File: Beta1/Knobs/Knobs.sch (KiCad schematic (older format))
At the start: 32 parts, among them U1000 MCP3008T-I/SL, U2 MCP3008T-I/SL

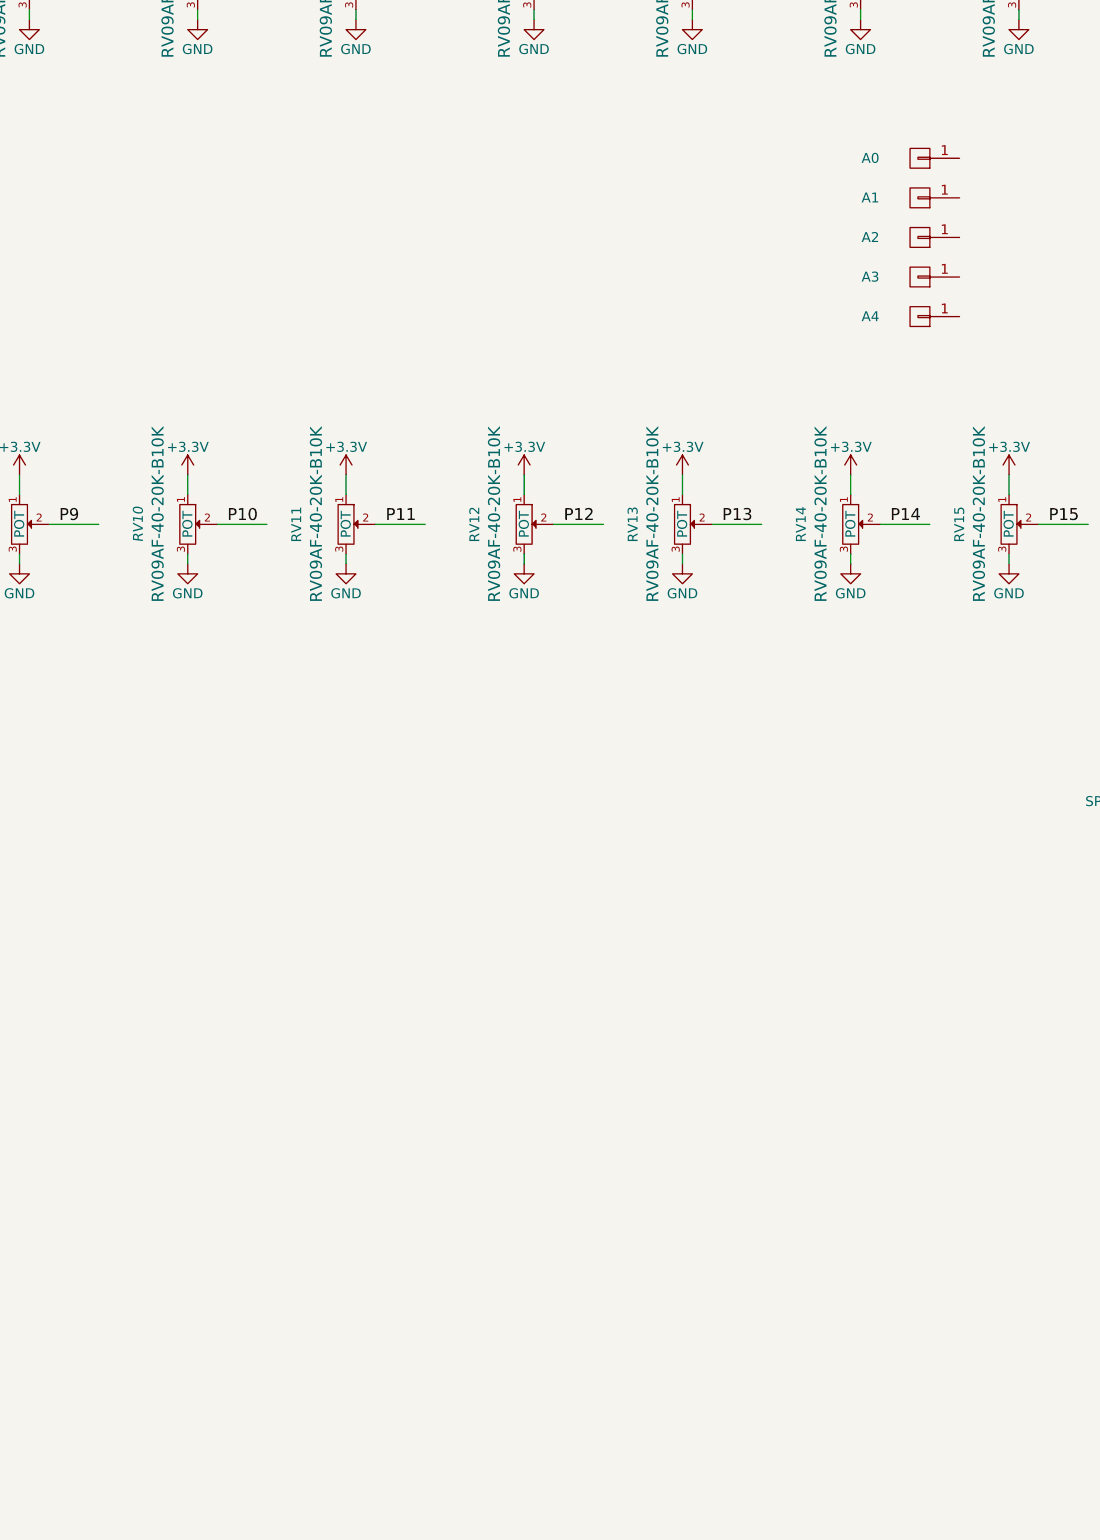
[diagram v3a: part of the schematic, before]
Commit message: Added volume knob + XY Joy to Knobs 16 CH Board.
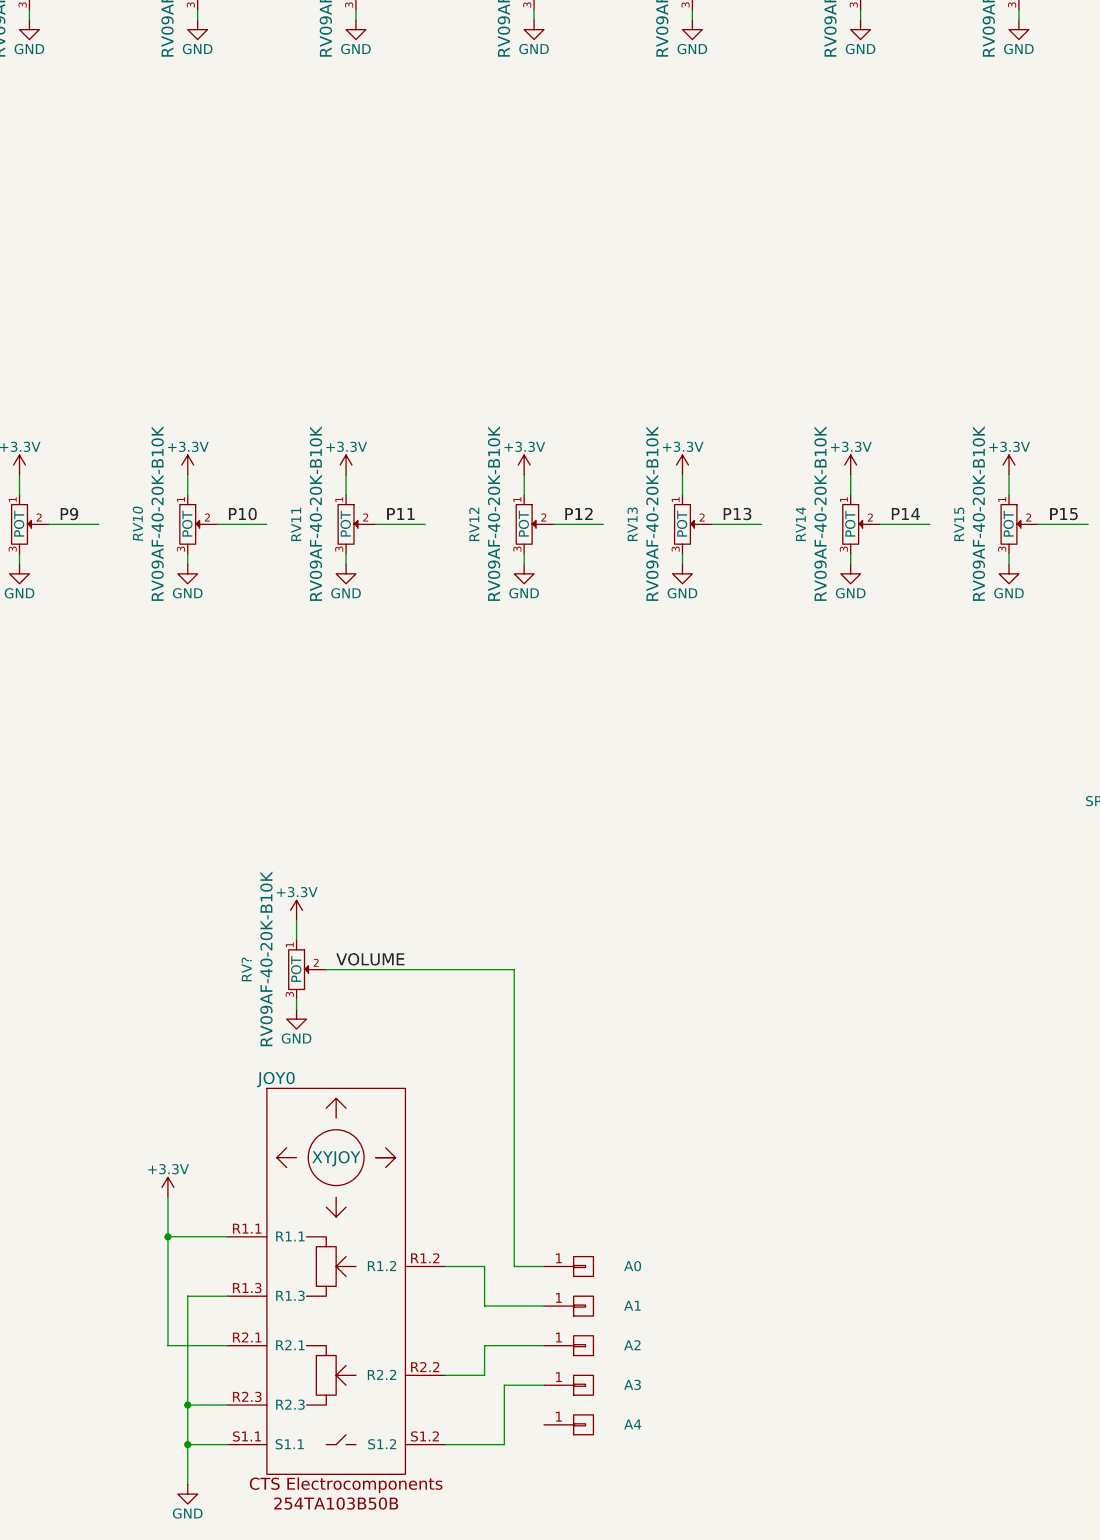
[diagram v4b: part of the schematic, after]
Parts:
- added JOY0: XYJOY, Liberry:XY_JOY_254TA103B50B, symbol XYJOY
- added RV?: POT, Liberry:RV09AF-40-20K-B10K, symbol POT
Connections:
- net labels added: VOLUME
- wire segments 92 -> 113
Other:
- moved on the sheet: A0, A1, A2, A3, A4
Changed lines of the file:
@@
 Text Label 11350 1750 0    60   ~ 0
 MISO
+Text Label 11450 4500 0    60   ~ 0
+MISO
+$Comp
+L CONN_01X01 A0
+U 1 1 58336F43
+P 5750 8050
+F 0 "A0" H 6000 8050 50  0000 C CNN
+F 1 "CONN_01X01" V 5850 8050 50  0001 C CNN
+F 2 "Liberry:TH_0.1_1x2_Jumper" H 5750 8050 50  0001 C CNN
+F 3 "" H 5750 8050 50  0000 C CNN
+F 4 "PCB" H 5750 8050 60  0001 C CNN "MFG"
+F 5 "ON_PCB" H 5750 8050 60  0001 C CNN "MPN"
+	1    5750 8050
+	1    0    0    1
+$EndComp
+$Comp
+L CONN_01X01 A1
+U 1 1 5833717C
+P 5750 8250
+F 0 "A1" H 6000 8250 50  0000 C CNN
+F 1 "CONN_01X01" V 5850 8250 50  0001 C CNN
+F 2 "Liberry:TH_0.1_1x2_Jumper" H 5750 8250 50  0001 C CNN
+F 3 "" H 5750 8250 50  0000 C CNN
+F 4 "PCB" H 5750 8250 60  0001 C CNN "MFG"
+F 5 "ON_PCB" H 5750 8250 60  0001 C CNN "MPN"
+	1    5750 8250
+	1    0    0    1
+$EndComp
+$Comp
+L CONN_01X01 A2
+U 1 1 58337609
+P 5750 8450
+F 0 "A2" H 6000 8450 50  0000 C CNN
+F 1 "CONN_01X01" V 5850 8450 50  0001 C CNN
+F 2 "Liberry:TH_0.1_1x2_Jumper" H 5750 8450 50  0001 C CNN
+F 3 "" H 5750 8450 50  0000 C CNN
+F 4 "PCB" H 5750 8450 60  0001 C CNN "MFG"
+F 5 "ON_PCB" H 5750 8450 60  0001 C CNN "MPN"
+	1    5750 8450
+	1    0    0    1
+$EndComp
+$Comp
+L CONN_01X01 A3
+U 1 1 58337619
+P 5750 8650
+F 0 "A3" H 6000 8650 50  0000 C CNN
+F 1 "CONN_01X01" V 5850 8650 50  0001 C CNN
+F 2 "Liberry:TH_0.1_1x2_Jumper" H 5750 8650 50  0001 C CNN
+F 3 "" H 5750 8650 50  0000 C CNN
+F 4 "PCB" H 5750 8650 60  0001 C CNN "MFG"
+F 5 "ON_PCB" H 5750 8650 60  0001 C CNN "MPN"
+	1    5750 8650
+	1    0    0    1
+$EndComp
+$Comp
+L CONN_01X01 A4
+U 1 1 58337C21
+P 5750 8850
+F 0 "A4" H 6000 8850 50  0000 C CNN
+F 1 "CONN_01X01" V 5850 8850 50  0001 C CNN
+F 2 "Liberry:TH_0.1_1x2_Jumper" H 5750 8850 50  0001 C CNN
+F 3 "" H 5750 8850 50  0000 C CNN
+F 4 "PCB" H 5750 8850 60  0001 C CNN "MFG"
+F 5 "ON_PCB" H 5750 8850 60  0001 C CNN "MPN"
+	1    5750 8850
+	1    0    0    1
+$EndComp
+$Comp
+L XYJOY JOY0
+U 1 1 5880F7E5
+P 4500 8050
+F 0 "JOY0" H 4200 9000 60  0000 C CNN
+F 1 "XYJOY" H 4500 8600 60  0000 C CNN
+F 2 "Liberry:XY_JOY_254TA103B50B" H 4500 8600 60  0001 C CNN
+F 3 "" H 4500 8600 60  0001 C CNN
+	1    4500 8050
+	1    0    0    -1
+$EndComp
+$Comp
+L +3.3V #PWR?
+U 1 1 5880F86D
+P 3650 7700
+F 0 "#PWR?" H 3650 7550 50  0001 C CNN
+F 1 "+3.3V" H 3650 7840 50  0000 C CNN
+F 2 "" H 3650 7700 50  0000 C CNN
+F 3 "" H 3650 7700 50  0000 C CNN
+	1    3650 7700
+	1    0    0    -1
+$EndComp
+$Comp
+L GND #PWR?
+U 1 1 5880F8DB
+P 3750 9150
+F 0 "#PWR?" H 3750 8900 50  0001 C CNN
+F 1 "GND" H 3750 9000 50  0000 C CNN
+F 2 "" H 3750 9150 50  0000 C CNN
+F 3 "" H 3750 9150 50  0000 C CNN
+	1    3750 9150
+	1    0    0    -1
+$EndComp
 Wire Wire Line
 	2150 1400 2150 1300
@@
 Wire Wire Line
 	11150 4500 12000 4500
-Text Label 11450 4500 0    60   ~ 0
-MISO
-$Comp
-L CONN_01X01 A0
-U 1 1 58336F43
-P 7450 2450
-F 0 "A0" H 7700 2450 50  0000 C CNN
-F 1 "CONN_01X01" V 7550 2450 50  0001 C CNN
-F 2 "Liberry:TH_0.1_1x2_Jumper" H 7450 2450 50  0001 C CNN
-F 3 "" H 7450 2450 50  0000 C CNN
-F 4 "PCB" H 7450 2450 60  0001 C CNN "MFG"
-F 5 "ON_PCB" H 7450 2450 60  0001 C CNN "MPN"
-	1    7450 2450
-	-1   0    0    1
-$EndComp
-$Comp
-L CONN_01X01 A1
-U 1 1 5833717C
-P 7450 2650
-F 0 "A1" H 7700 2650 50  0000 C CNN
-F 1 "CONN_01X01" V 7550 2650 50  0001 C CNN
-F 2 "Liberry:TH_0.1_1x2_Jumper" H 7450 2650 50  0001 C CNN
-F 3 "" H 7450 2650 50  0000 C CNN
-F 4 "PCB" H 7450 2650 60  0001 C CNN "MFG"
-F 5 "ON_PCB" H 7450 2650 60  0001 C CNN "MPN"
-	1    7450 2650
-	-1   0    0    1
-$EndComp
-$Comp
-L CONN_01X01 A2
-U 1 1 58337609
-P 7450 2850
-F 0 "A2" H 7700 2850 50  0000 C CNN
-F 1 "CONN_01X01" V 7550 2850 50  0001 C CNN
-F 2 "Liberry:TH_0.1_1x2_Jumper" H 7450 2850 50  0001 C CNN
-F 3 "" H 7450 2850 50  0000 C CNN
-F 4 "PCB" H 7450 2850 60  0001 C CNN "MFG"
-F 5 "ON_PCB" H 7450 2850 60  0001 C CNN "MPN"
-	1    7450 2850
-	-1   0    0    1
-$EndComp
-$Comp
-L CONN_01X01 A3
-U 1 1 58337619
-P 7450 3050
-F 0 "A3" H 7700 3050 50  0000 C CNN
-F 1 "CONN_01X01" V 7550 3050 50  0001 C CNN
-F 2 "Liberry:TH_0.1_1x2_Jumper" H 7450 3050 50  0001 C CNN
-F 3 "" H 7450 3050 50  0000 C CNN
-F 4 "PCB" H 7450 3050 60  0001 C CNN "MFG"
-F 5 "ON_PCB" H 7450 3050 60  0001 C CNN "MPN"
-	1    7450 3050
-	-1   0    0    1
-$EndComp
-$Comp
-L CONN_01X01 A4
-U 1 1 58337C21
-P 7450 3250
-F 0 "A4" H 7700 3250 50  0000 C CNN
-F 1 "CONN_01X01" V 7550 3250 50  0001 C CNN
-F 2 "Liberry:TH_0.1_1x2_Jumper" H 7450 3250 50  0001 C CNN
-F 3 "" H 7450 3250 50  0000 C CNN
-F 4 "PCB" H 7450 3250 60  0001 C CNN "MFG"
-F 5 "ON_PCB" H 7450 3250 60  0001 C CNN "MPN"
-	1    7450 3250
-	-1   0    0    1
-$EndComp
+Wire Wire Line
+	3950 7900 3650 7900
+Wire Wire Line
+	3650 7700 3650 8450
+Wire Wire Line
+	3650 8450 3950 8450
+Connection ~ 3650 7900
+Wire Wire Line
+	3950 8200 3750 8200
+Wire Wire Line
+	3750 8200 3750 9150
+Wire Wire Line
+	3950 8750 3750 8750
+Connection ~ 3750 8750
+Wire Wire Line
+	3950 8950 3750 8950
+Connection ~ 3750 8950
+$Comp
+L POT RV?
+U 1 1 58810DA5
+P 4300 6550
+F 0 "RV?" H 4300 6300 50  0000 C CNN
+F 1 "POT" H 4300 6550 50  0000 C CNN
+F 2 "Liberry:RV09AF-40-20K-B10K" H 4300 6550 50  0001 C CNN
+F 3 "" H 4300 6550 50  0000 C CNN
+F 4 "Alpha Taiwan" H 4300 6550 60  0001 C CNN "MFG"
+F 5 "RV09AF-40-20K-B10K" H 4250 6400 60  0000 C CNN "MPN"
+	1    4300 6550
+	0    1    1    0
+$EndComp
+$Comp
+L GND #PWR?
+U 1 1 58810DAB
+P 4300 6750
+F 0 "#PWR?" H 4300 6500 50  0001 C CNN
+F 1 "GND" H 4300 6600 50  0000 C CNN
+F 2 "" H 4300 6750 50  0000 C CNN
+F 3 "" H 4300 6750 50  0000 C CNN
+	1    4300 6750
+	1    0    0    -1
+$EndComp
+$Comp
+L +3.3V #PWR?
+U 1 1 58810DB1
+P 4300 6300
+F 0 "#PWR?" H 4300 6150 50  0001 C CNN
+F 1 "+3.3V" H 4300 6440 50  0000 C CNN
+F 2 "" H 4300 6300 50  0000 C CNN
+F 3 "" H 4300 6300 50  0000 C CNN
+	1    4300 6300
+	1    0    0    -1
+$EndComp
+Text Label 4500 6550 0    60   ~ 0
+VOLUME
+Wire Wire Line
+	4300 6400 4300 6300
+Wire Wire Line
+	4300 6750 4300 6700
+Wire Wire Line
+	4450 6550 5400 6550
+Wire Wire Line
+	5400 6550 5400 8050
+Wire Wire Line
+	5400 8050 5550 8050
+Wire Wire Line
+	5050 8050 5250 8050
+Wire Wire Line
+	5250 8050 5250 8250
+Wire Wire Line
+	5250 8250 5550 8250
+Wire Wire Line
+	5050 8600 5250 8600
+Wire Wire Line
+	5250 8600 5250 8450
+Wire Wire Line
+	5250 8450 5550 8450
+Wire Wire Line
+	5050 8950 5350 8950
+Wire Wire Line
+	5350 8950 5350 8650
+Wire Wire Line
+	5350 8650 5550 8650
 $EndSCHEMATC

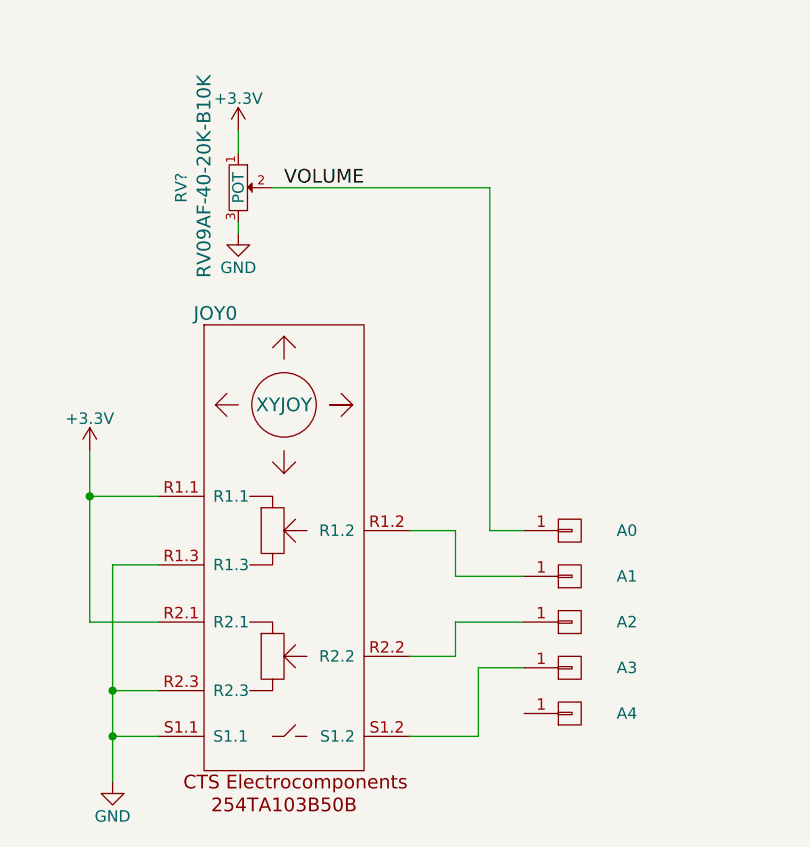
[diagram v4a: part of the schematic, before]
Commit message: Reduced width by 5.08. Changed pinout location and organization
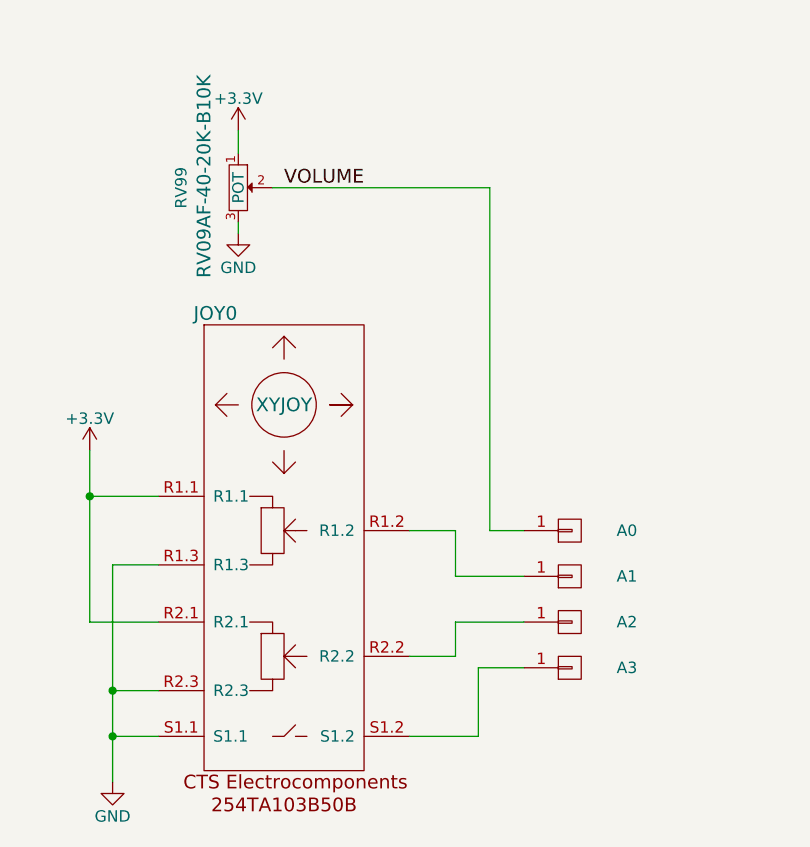
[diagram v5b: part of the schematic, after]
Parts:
- removed A4: CONN_01X01, Liberry:TH_0.1_1x2_Jumper, symbol CONN_01X01
- A0, A1, A2, A3: footprint Liberry:TH_0.1_1x2_Jumper -> Liberry:single_0.1
- gave numbers to parts that had none: 1
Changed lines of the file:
@@
 F 0 "A0" H 6000 8050 50  0000 C CNN
 F 1 "CONN_01X01" V 5850 8050 50  0001 C CNN
-F 2 "Liberry:TH_0.1_1x2_Jumper" H 5750 8050 50  0001 C CNN
+F 2 "Liberry:single_0.1" H 5750 8050 50  0001 C CNN
 F 3 "" H 5750 8050 50  0000 C CNN
 F 4 "PCB" H 5750 8050 60  0001 C CNN "MFG"
@@
 F 0 "A1" H 6000 8250 50  0000 C CNN
 F 1 "CONN_01X01" V 5850 8250 50  0001 C CNN
-F 2 "Liberry:TH_0.1_1x2_Jumper" H 5750 8250 50  0001 C CNN
+F 2 "Liberry:single_0.1" H 5750 8250 50  0001 C CNN
 F 3 "" H 5750 8250 50  0000 C CNN
 F 4 "PCB" H 5750 8250 60  0001 C CNN "MFG"
@@
 F 0 "A2" H 6000 8450 50  0000 C CNN
 F 1 "CONN_01X01" V 5850 8450 50  0001 C CNN
-F 2 "Liberry:TH_0.1_1x2_Jumper" H 5750 8450 50  0001 C CNN
+F 2 "Liberry:single_0.1" H 5750 8450 50  0001 C CNN
 F 3 "" H 5750 8450 50  0000 C CNN
 F 4 "PCB" H 5750 8450 60  0001 C CNN "MFG"
@@
 F 0 "A3" H 6000 8650 50  0000 C CNN
 F 1 "CONN_01X01" V 5850 8650 50  0001 C CNN
-F 2 "Liberry:TH_0.1_1x2_Jumper" H 5750 8650 50  0001 C CNN
+F 2 "Liberry:single_0.1" H 5750 8650 50  0001 C CNN
 F 3 "" H 5750 8650 50  0000 C CNN
 F 4 "PCB" H 5750 8650 60  0001 C CNN "MFG"
 F 5 "ON_PCB" H 5750 8650 60  0001 C CNN "MPN"
 	1    5750 8650
-	1    0    0    1
-$EndComp
-$Comp
-L CONN_01X01 A4
-U 1 1 58337C21
-P 5750 8850
-F 0 "A4" H 6000 8850 50  0000 C CNN
-F 1 "CONN_01X01" V 5850 8850 50  0001 C CNN
-F 2 "Liberry:TH_0.1_1x2_Jumper" H 5750 8850 50  0001 C CNN
-F 3 "" H 5750 8850 50  0000 C CNN
-F 4 "PCB" H 5750 8850 60  0001 C CNN "MFG"
-F 5 "ON_PCB" H 5750 8850 60  0001 C CNN "MPN"
-	1    5750 8850
 	1    0    0    1
 $EndComp
@@
 $EndComp
 $Comp
-L +3.3V #PWR?
+L +3.3V #PWR039
 U 1 1 5880F86D
 P 3650 7700
-F 0 "#PWR?" H 3650 7550 50  0001 C CNN
+F 0 "#PWR039" H 3650 7550 50  0001 C CNN
 F 1 "+3.3V" H 3650 7840 50  0000 C CNN
 F 2 "" H 3650 7700 50  0000 C CNN
@@
 $EndComp
 $Comp
-L GND #PWR?
+L GND #PWR040
 U 1 1 5880F8DB
 P 3750 9150
-F 0 "#PWR?" H 3750 8900 50  0001 C CNN
+F 0 "#PWR040" H 3750 8900 50  0001 C CNN
 F 1 "GND" H 3750 9000 50  0000 C CNN
 F 2 "" H 3750 9150 50  0000 C CNN
@@
 Connection ~ 3750 8950
 $Comp
-L POT RV?
+L POT RV99
 U 1 1 58810DA5
 P 4300 6550
-F 0 "RV?" H 4300 6300 50  0000 C CNN
+F 0 "RV99" H 4300 6300 50  0000 C CNN
 F 1 "POT" H 4300 6550 50  0000 C CNN
 F 2 "Liberry:RV09AF-40-20K-B10K" H 4300 6550 50  0001 C CNN
@@
 $EndComp
 $Comp
-L GND #PWR?
+L GND #PWR041
 U 1 1 58810DAB
 P 4300 6750
-F 0 "#PWR?" H 4300 6500 50  0001 C CNN
+F 0 "#PWR041" H 4300 6500 50  0001 C CNN
 F 1 "GND" H 4300 6600 50  0000 C CNN
 F 2 "" H 4300 6750 50  0000 C CNN
@@
 $EndComp
 $Comp
-L +3.3V #PWR?
+L +3.3V #PWR042
 U 1 1 58810DB1
 P 4300 6300
-F 0 "#PWR?" H 4300 6150 50  0001 C CNN
+F 0 "#PWR042" H 4300 6150 50  0001 C CNN
 F 1 "+3.3V" H 4300 6440 50  0000 C CNN
 F 2 "" H 4300 6300 50  0000 C CNN
